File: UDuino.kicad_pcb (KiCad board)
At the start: 2 copper layers, 31 parts, among them J1 Screw_Terminal_01x04, U1 NAU8315YG, U2 DRV8833RTY, U3 NAU8315YG, U4 STM32L452VCTx

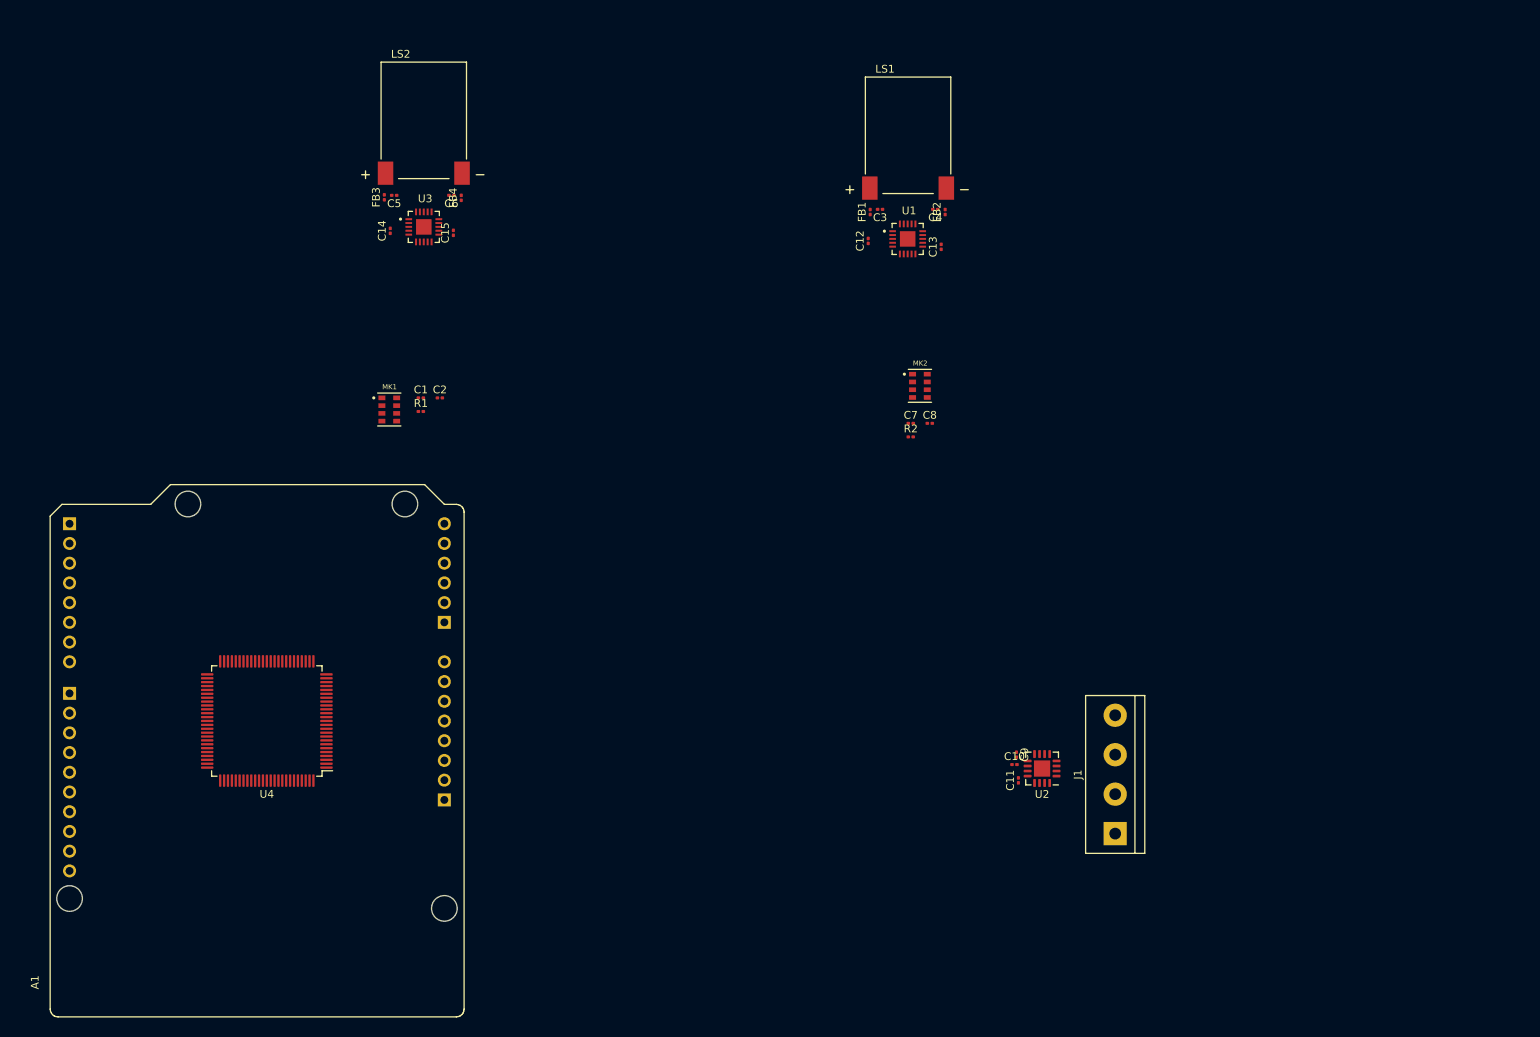
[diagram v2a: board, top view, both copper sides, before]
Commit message: Added Switches, Buttons, LEDs, 7Seg, LCD
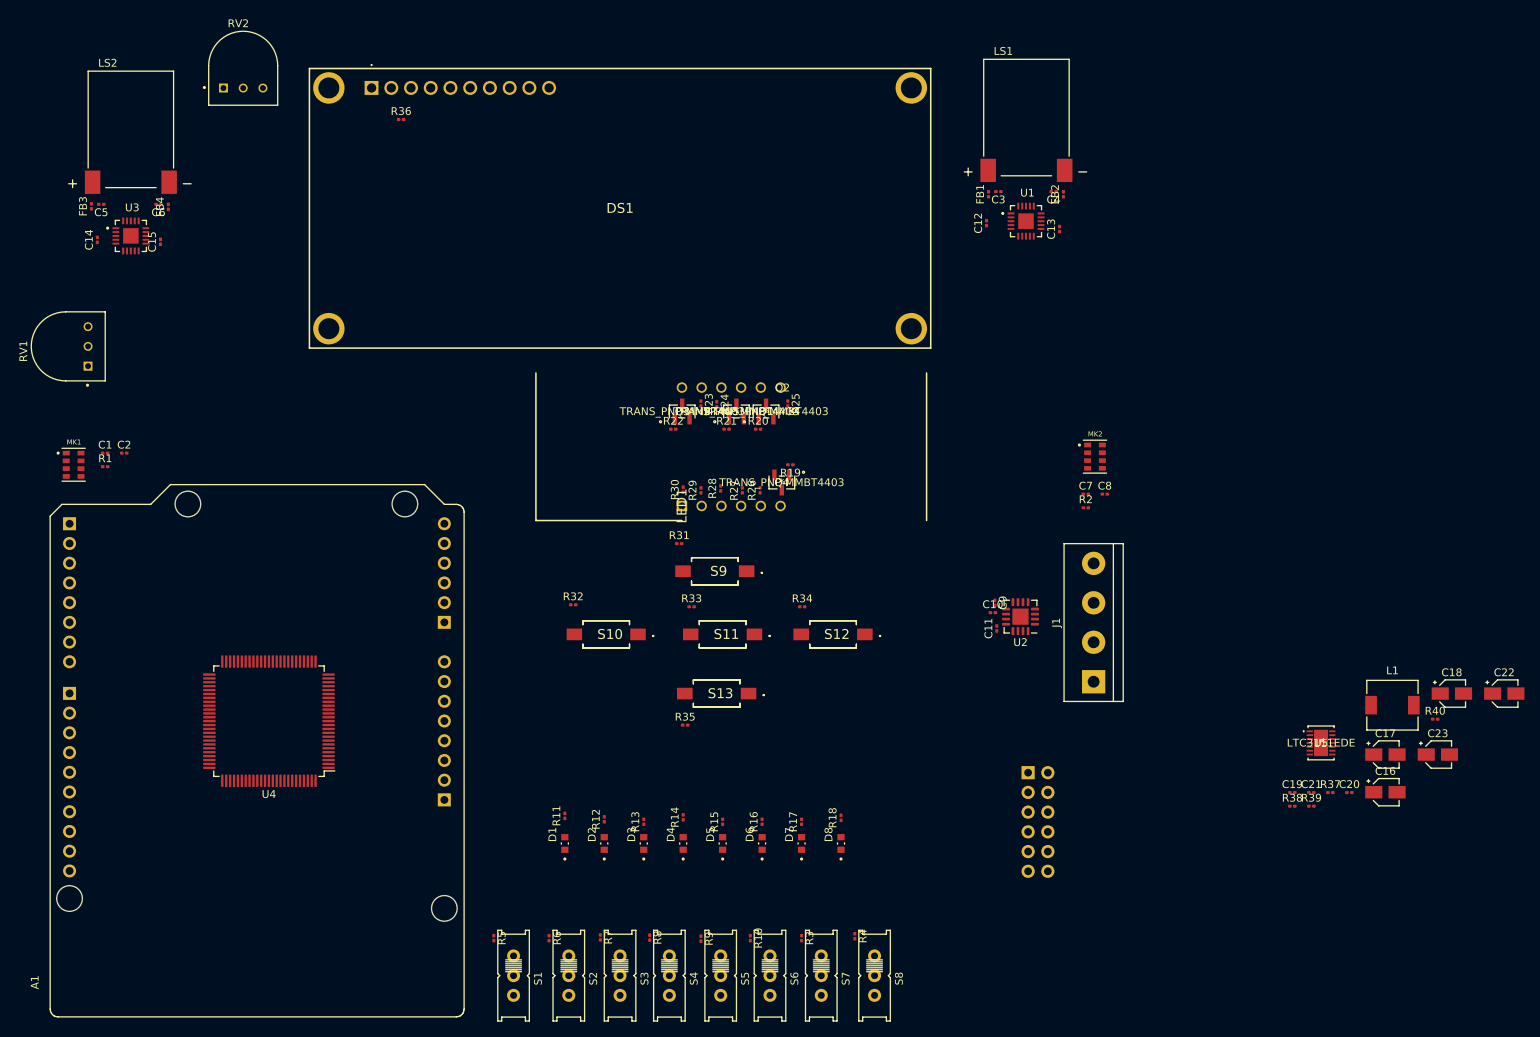
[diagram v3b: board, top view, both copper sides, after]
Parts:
- added C16: 27pF, Capacitor_SMD:CP_Elec_3x5.3, F.Cu at (201.2, 127.3)
- added C17: 600pF, Capacitor_SMD:CP_Elec_3x5.3, F.Cu at (201.2, 122.4)
- added C18: 27pF, Capacitor_SMD:CP_Elec_3x5.3, F.Cu at (209.7, 114.6)
- added C19: 0u1, Capacitor_SMD:C_0201_0603Metric, F.Cu at (189.2, 127.3)
- added C20: 0u1, Capacitor_SMD:C_0201_0603Metric, F.Cu at (196.5, 127.3)
- added C21: 1µF, Capacitor_SMD:C_0201_0603Metric, F.Cu at (191.6, 127.3)
- added C22: 33pF, Capacitor_SMD:CP_Elec_3x5.3, F.Cu at (216.5, 114.6)
- added C23: 22µF, Capacitor_SMD:CP_Elec_3x5.3, F.Cu at (207.9, 122.4)
- added D1: LTST-C190KRKT, Custom:LEDC1608X35N, F.Cu at (95.5, 133.9)
- added D2: LTST-C190KRKT, Custom:LEDC1608X35N, F.Cu at (100.6, 133.9)
- added D3: LTST-C190KRKT, Custom:LEDC1608X35N, F.Cu at (105.7, 133.9)
- added D4: LTST-C190KRKT, Custom:LEDC1608X35N, F.Cu at (110.7, 133.9)
- added D5: LTST-C190KRKT, Custom:LEDC1608X35N, F.Cu at (115.8, 133.9)
- added D6: LTST-C190KRKT, Custom:LEDC1608X35N, F.Cu at (120.9, 133.9)
- added D7: LTST-C190KRKT, Custom:LEDC1608X35N, F.Cu at (126.0, 133.9)
- added D8: LTST-C190KRKT, Custom:LEDC1608X35N, F.Cu at (131.1, 133.9)
- added DS1: AMC1602AR-B-Y6WFDY-SPI, Custom:AMC1602ARBY6WFDYSPI, F.Cu at (70.6, 36.6)
- added J2: PMOD1, Connector_PinSocket_2.54mm:PinSocket_2x06_P2.54mm_Horizontal, B.Cu at (155.2, 124.7)
- added L1: 4u7, Inductor_SMD:L_6.3x6.3_H3, F.Cu at (202.1, 116.1)
- added LED1: LDQ-M516RI, Custom:DIPS1524W50P254L5030H800Q12N, F.Cu at (110.6, 90.4)
- added Q1: TRANS_PNP-MMBT4403, Custom:MMBT4403LT3G, F.Cu at (121.4, 78.2)
- added Q2: TRANS_PNP-MMBT4403, Custom:MMBT4403LT3G, F.Cu at (117.6, 78.2)
- added Q3: TRANS_PNP-MMBT4403, Custom:MMBT4403LT3G, F.Cu at (110.6, 78.2)
- added Q4: TRANS_PNP-MMBT4403, Custom:MMBT4403LT3G, F.Cu at (123.4, 87.4)
- added R10: 10k, Resistor_SMD:R_0201_0603Metric, F.Cu at (119.4, 146.1)
- added R11: 220, Resistor_SMD:R_0201_0603Metric, F.Cu at (95.5, 130.3)
- added R12: 220, Resistor_SMD:R_0201_0603Metric, F.Cu at (100.6, 130.7)
- added R13: 220, Resistor_SMD:R_0201_0603Metric, F.Cu at (105.7, 131.1)
- added R14: 220, Resistor_SMD:R_0201_0603Metric, F.Cu at (110.7, 130.5)
- added R15: 220, Resistor_SMD:R_0201_0603Metric, F.Cu at (115.8, 131.1)
- added R16: 220, Resistor_SMD:R_0201_0603Metric, F.Cu at (120.9, 131.1)
- added R17: 220, Resistor_SMD:R_0201_0603Metric, F.Cu at (126.0, 131.1)
- added R18: 220, Resistor_SMD:R_0201_0603Metric, F.Cu at (131.1, 130.6)
- added R19: 1k, Resistor_SMD:R_0201_0603Metric, F.Cu at (124.6, 85.1)
- added R20: 1k, Resistor_SMD:R_0201_0603Metric, F.Cu at (120.4, 80.5)
- added R21: 1k, Resistor_SMD:R_0201_0603Metric, F.Cu at (116.3, 80.5)
- added R22: 1k, Resistor_SMD:R_0201_0603Metric, F.Cu at (109.5, 80.5)
- added R23: 220, Resistor_SMD:R_0201_0603Metric, F.Cu at (113.0, 77.2)
- added R24: 220, Resistor_SMD:R_0201_0603Metric, F.Cu at (115.1, 77.3)
- added R25: 220, Resistor_SMD:R_0201_0603Metric, F.Cu at (124.2, 77.2)
- added R26: 220, Resistor_SMD:R_0201_0603Metric, F.Cu at (120.7, 88.4)
- added R27: 220, Resistor_SMD:R_0201_0603Metric, F.Cu at (118.4, 88.4)
- added R28: 220, Resistor_SMD:R_0201_0603Metric, F.Cu at (115.6, 88.1)
- added R29: 220, Resistor_SMD:R_0201_0603Metric, F.Cu at (113.0, 88.4)
- added R3: 10k, Resistor_SMD:R_0201_0603Metric, F.Cu at (126.0, 146.1)
- added R30: 220, Resistor_SMD:R_0201_0603Metric, F.Cu at (110.7, 88.3)
- added R31: 10k, Resistor_SMD:R_0201_0603Metric, F.Cu at (110.2, 95.2)
- added R32: 10k, Resistor_SMD:R_0201_0603Metric, F.Cu at (96.6, 103.1)
- added R33: 10k, Resistor_SMD:R_0201_0603Metric, F.Cu at (111.8, 103.4)
- added R34: 10k, Resistor_SMD:R_0201_0603Metric, F.Cu at (126.1, 103.4)
- added R35: 10k, Resistor_SMD:R_0201_0603Metric, F.Cu at (111.0, 118.6)
- added R36: 50, Resistor_SMD:R_0201_0603Metric, F.Cu at (74.4, 40.6)
- added R37: 26.1k, Resistor_SMD:R_0201_0603Metric, F.Cu at (194.1, 127.3)
- added R38: 57.6k, Resistor_SMD:R_0201_0603Metric, F.Cu at (189.2, 129.1)
- added R39: 1M, Resistor_SMD:R_0201_0603Metric, F.Cu at (191.6, 129.1)
- added R4: 10k, Resistor_SMD:R_0201_0603Metric, F.Cu at (132.8, 145.8)
- added R40: 20k, Resistor_SMD:R_0201_0603Metric, F.Cu at (207.6, 117.9)
- added R5: 10k, Resistor_SMD:R_0201_0603Metric, F.Cu at (86.4, 146.1)
- added R6: 10k, Resistor_SMD:R_0201_0603Metric, F.Cu at (93.5, 146.1)
- added R7: 10k, Resistor_SMD:R_0201_0603Metric, F.Cu at (100.1, 146.0)
- added R8: 10k, Resistor_SMD:R_0201_0603Metric, F.Cu at (106.4, 146.0)
- added R9: 10k, Resistor_SMD:R_0201_0603Metric, F.Cu at (113.0, 146.1)
- added RV1: R_Potentiometer, Custom:TRIM_3352T-1-104LF, F.Cu at (31.2, 69.8)
- added RV2: 100k, Custom:TRIM_3352T-1-104LF, F.Cu at (54.1, 33.7)
- added S1: EG1218, Custom:EG1218, F.Cu at (88.9, 150.9)
- added S10: PTS636_SM43_SMTR_LFS, Custom:PTS636SM43SMTRLFS, F.Cu at (100.8, 106.9)
- added S11: PTS636_SM43_SMTR_LFS, Custom:PTS636SM43SMTRLFS, F.Cu at (115.8, 106.9)
- added S12: PTS636_SM43_SMTR_LFS, Custom:PTS636SM43SMTRLFS, F.Cu at (130.0, 106.9)
- added S13: PTS636_SM43_SMTR_LFS, Custom:PTS636SM43SMTRLFS, F.Cu at (115.1, 114.6)
- added S2: EG1218, Custom:EG1218, F.Cu at (96.0, 150.9)
- added S3: EG1218, Custom:EG1218, F.Cu at (102.6, 150.9)
- added S4: EG1218, Custom:EG1218, F.Cu at (109.0, 150.9)
- added S5: EG1218, Custom:EG1218, F.Cu at (115.6, 150.9)
- added S6: EG1218, Custom:EG1218, F.Cu at (121.9, 150.9)
- added S7: EG1218, Custom:EG1218, F.Cu at (128.5, 150.9)
- added S8: EG1218, Custom:EG1218, F.Cu at (135.4, 150.9)
- added S9: PTS636_SM43_SMTR_LFS, Custom:PTS636SM43SMTRLFS, F.Cu at (114.8, 98.8)
- added U5: LTC3111EDE, Custom:LTC3111EDE-TRPBF, F.Cu at (192.9, 120.9)
- moved C2 41.3 mm to (38.8, 83.6)
- moved C1 41.3 mm to (36.3, 83.6)
- moved R1 41.3 mm to (36.3, 85.3)
- moved MK1 41.3 mm to (32.3, 85.1)
- moved C5 37.7 mm to (35.8, 51.6)
- moved C6 37.7 mm to (43.2, 51.6)
- moved C14 37.7 mm to (35.3, 56.1)
- moved C15 37.7 mm to (43.4, 56.4)
- moved FB3 37.7 mm to (34.5, 51.8)
- moved FB4 37.7 mm to (44.5, 51.9)
- moved LS2 37.7 mm to (39.6, 41.9)
- moved U3 37.7 mm to (39.6, 55.6)
- moved MK2 24.3 mm to (163.8, 84.0)
- moved C7 24.3 mm to (162.6, 88.9)
- moved C8 24.3 mm to (165.0, 88.9)
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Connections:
- net Net-(A1-PadA0) renamed /A0
- net Net-(A1-PadA1) renamed /A1
- net Net-(A1-PadA2) renamed /A2
- net Net-(A1-PadA3) renamed /A3
- net Net-(A1-PadA4) renamed /A4
- net Net-(A1-PadA4)_1 renamed /I2C4_SDA
- net Net-(A1-PadA5) renamed /A5
- net Net-(A1-PadA5)_1 renamed /I2C4_SCL
- net Net-(A1-PadD2) renamed /D2
- net Net-(A1-PadD3) renamed /D3
- net Net-(A1-PadD4) renamed /D4
- net Net-(A1-PadD5) renamed /D5
- net Net-(U4-Pad45) renamed /D6
- net Net-(U4-Pad46) renamed /D7
- A1 pad 3V3: unconnected-(A1-Pad3V3) -> +3V3
- A1 pad 5V: unconnected-(A1-Pad5V) -> +5V
- A1 pad GND_1: unconnected-(A1-PadGND_1) -> GND
- A1 pad GND_2: unconnected-(A1-PadGND_2) -> GND
- MK1 pad 3: /SIA1_FS_B -> /SAI1_FS_A
- MK1 pad 6: /SIA1_SCK_B -> /SAI1_SCK_A
- MK2 pad 3: /SIA1_FS_B -> /SAI1_FS_A
- MK2 pad 6: /SIA1_SCK_B -> /SAI1_SCK_A
- U3 pad 13: /Speaker Right/GAIN -> /Speaker Left/GAIN
- U4 pad 1: unconnected-(U4-Pad1) -> /Motor/BIN2
- U4 pad 10: unconnected-(U4-Pad10) -> GND
- U4 pad 100: unconnected-(U4-Pad100) -> +3V3
- U4 pad 11: unconnected-(U4-Pad11) -> +3V3
- U4 pad 15: /Motor/AIN1 -> /LEDs/LED1
- U4 pad 16: /Motor/AIN2 -> /LEDs/LED2
- U4 pad 17: /Motor/BIN2 -> /LEDs/LED3
- U4 pad 18: /Motor/BIN1 -> /LEDs/LED4
- U4 pad 19: unconnected-(U4-Pad19) -> GND
- U4 pad 2: unconnected-(U4-Pad2) -> /Motor/BIN1
- U4 pad 22: unconnected-(U4-Pad22) -> +3V3
- U4 pad 27: unconnected-(U4-Pad27) -> GND
- U4 pad 28: unconnected-(U4-Pad28) -> +3V3
- U4 pad 33: unconnected-(U4-Pad33) -> /LEDs/LED5
- U4 pad 34: unconnected-(U4-Pad34) -> /LEDs/LED6
- U4 pad 35: unconnected-(U4-Pad35) -> /PMOD4
- U4 pad 36: unconnected-(U4-Pad36) -> /LCD/RS
- U4 pad 37: unconnected-(U4-Pad37) -> /LCD/CSB
- U4 pad 39: /SIA_SCK_B -> /PMOD_6
- U4 pad 40: /SIA1_FS_B -> /PMOD_7
- U4 pad 47: unconnected-(U4-Pad47) -> /Buttons/BT4
- U4 pad 48: unconnected-(U4-Pad48) -> /Buttons/BT5
- U4 pad 49: unconnected-(U4-Pad49) -> GND
- U4 pad 50: unconnected-(U4-Pad50) -> +3V3
- U4 pad 51: unconnected-(U4-Pad51) -> /7Seg/AN1
- U4 pad 52: unconnected-(U4-Pad52) -> /7Seg/AN2
- U4 pad 53: unconnected-(U4-Pad53) -> /7Seg/AN3
- U4 pad 54: unconnected-(U4-Pad54) -> /7Seg/AN4
- U4 pad 6: unconnected-(U4-Pad6) -> +3V3
- U4 pad 63: unconnected-(U4-Pad63) -> /LEDs/LED7
- U4 pad 64: unconnected-(U4-Pad64) -> /LEDs/LED8
- U4 pad 65: unconnected-(U4-Pad65) -> /7Seg/A
- U4 pad 66: unconnected-(U4-Pad66) -> /7Seg/B
- U4 pad 67: unconnected-(U4-Pad67) -> /PMOD_1
- U4 pad 68: unconnected-(U4-Pad68) -> /PMOD2
- U4 pad 69: unconnected-(U4-Pad69) -> /PMOD_3
- U4 pad 7: unconnected-(U4-Pad7) -> /7Seg/F
- U4 pad 70: unconnected-(U4-Pad70) -> /USB_DM
- U4 pad 71: unconnected-(U4-Pad71) -> /USB_DP
- U4 pad 72: unconnected-(U4-Pad72) -> /SYS_JTMS-SWDIO
- U4 pad 74: unconnected-(U4-Pad74) -> GND
- U4 pad 75: unconnected-(U4-Pad75) -> +3V3
- U4 pad 76: unconnected-(U4-Pad76) -> /SYS_JTCK-SWCLK
- U4 pad 77: unconnected-(U4-Pad77) -> /SYS_JTDI
- U4 pad 78: unconnected-(U4-Pad78) -> /7Seg/C
- U4 pad 79: unconnected-(U4-Pad79) -> /7Seg/D
- U4 pad 8: unconnected-(U4-Pad8) -> /7Seg/G
- U4 pad 80: unconnected-(U4-Pad80) -> /7Seg/E
- U4 pad 81: unconnected-(U4-Pad81) -> /SW1
- U4 pad 82: unconnected-(U4-Pad82) -> /SW2
- U4 pad 83: unconnected-(U4-Pad83) -> /SW3
- U4 pad 84: unconnected-(U4-Pad84) -> /SW4
- U4 pad 85: unconnected-(U4-Pad85) -> /SW5
- U4 pad 86: unconnected-(U4-Pad86) -> /SW6
- U4 pad 87: unconnected-(U4-Pad87) -> /SW7
- U4 pad 88: unconnected-(U4-Pad88) -> /SW8
- U4 pad 9: unconnected-(U4-Pad9) -> /7Seg/DP
- U4 pad 92: unconnected-(U4-Pad92) -> /PMOD_5
- U4 pad 93: unconnected-(U4-Pad93) -> /Buttons/BT1
- U4 pad 95: unconnected-(U4-Pad95) -> /Buttons/BT2
- U4 pad 96: unconnected-(U4-Pad96) -> /Buttons/BT3
- U4 pad 97: unconnected-(U4-Pad97) -> /Motor/AIN1
- U4 pad 98: unconnected-(U4-Pad98) -> /Motor/AIN2
- U4 pad 99: unconnected-(U4-Pad99) -> GND

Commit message: Update board design
5v and 3v3 power blocks wired up.
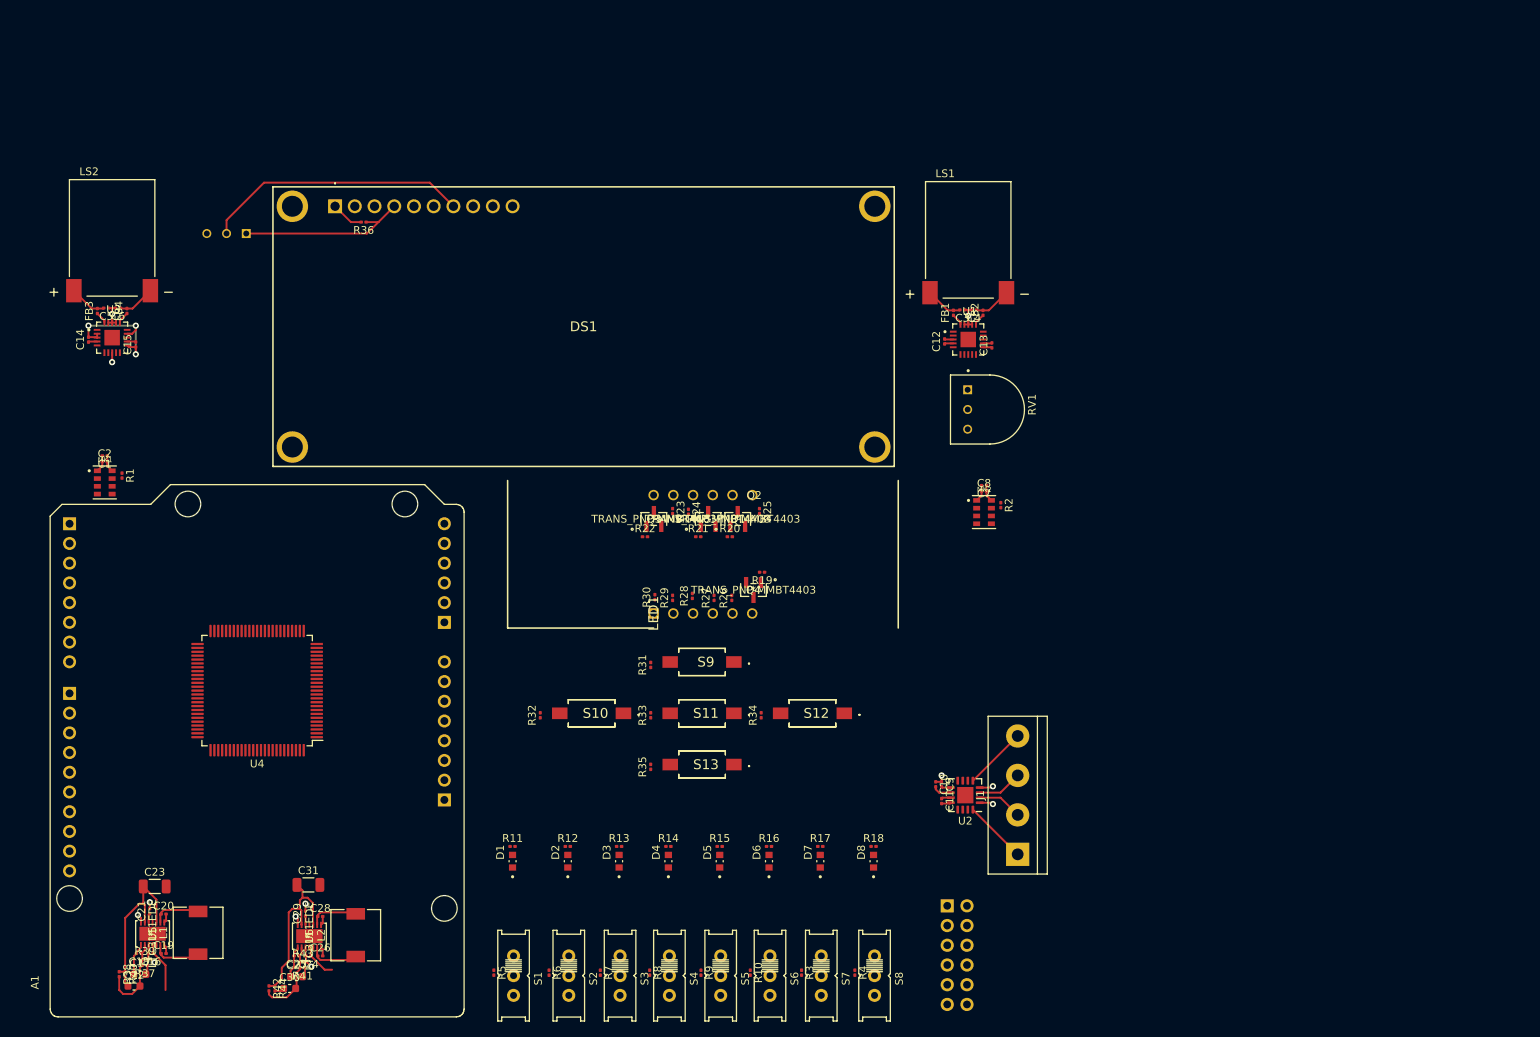
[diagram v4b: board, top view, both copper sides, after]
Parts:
- added C24: 27pF, Capacitor_SMD:C_0201_0603Metric, F.Cu at (62.5, 148.3)
- added C25: 27pF, Capacitor_SMD:C_0201_0603Metric, F.Cu at (61.0, 148.3)
- added C26: 0u1, Capacitor_SMD:C_0201_0603Metric, F.Cu at (64.0, 148.3)
- added C27: 680pF, Capacitor_SMD:C_0603_1608Metric, F.Cu at (61.0, 151.0)
- added C28: 0u1, Capacitor_SMD:C_0201_0603Metric, F.Cu at (64.0, 143.3)
- added C29: 1µF, Capacitor_SMD:C_0201_0603Metric, F.Cu at (62.1, 142.9)
- added C30: 33pF, Capacitor_SMD:C_0603_1608Metric, F.Cu at (60.1, 152.5)
- added C31: 22µF, Capacitor_SMD:C_1206_3216Metric, F.Cu at (62.5, 139.2)
- added L2: 4u7, Inductor_SMD:L_6.3x6.3_H3, F.Cu at (68.6, 145.7)
- added R41: 26.1k, Resistor_SMD:R_0201_0603Metric, F.Cu at (61.7, 149.9)
- added R42: 1M, Resistor_SMD:R_0201_0603Metric, F.Cu at (57.4, 152.5)
- added R43: 320k, Resistor_SMD:R_0201_0603Metric, F.Cu at (61.7, 149.1)
- added R44: 20k, Resistor_SMD:R_0201_0603Metric, F.Cu at (58.2, 152.5)
- added U6: LTC3111EDE, Custom:LTC3111EDE-TRPBF, F.Cu at (62.6, 145.8)
- C16, C18: footprint Capacitor_SMD:CP_Elec_3x5.3 -> Capacitor_SMD:C_0201_0603Metric
- C17: value 600pF -> 680pF; footprint Capacitor_SMD:CP_Elec_3x5.3 -> Capacitor_SMD:C_0603_1608Metric
- C22: footprint Capacitor_SMD:CP_Elec_3x5.3 -> Capacitor_SMD:C_0603_1608Metric
- C23: footprint Capacitor_SMD:CP_Elec_3x5.3 -> Capacitor_SMD:C_1206_3216Metric
- R38: value 57.6k -> 1M
- R39: value 1M -> 191k
- RV2: moved to B.Cu
- moved C22 180.4 mm to (40.0, 152.2)
- moved C18 172.3 mm to (40.7, 148.0), turned to 180 degrees
- moved R40 171.9 mm to (38.9, 150.7), turned to -90 degrees
- moved C23 166.1 mm to (42.7, 139.4)
- moved C17 162.9 mm to (40.8, 150.7)
- moved C16 160.3 mm to (42.2, 148.0), turned to 180 degrees
- moved L1 156.6 mm to (48.3, 145.4), turned to 90 degrees
- moved R37 154.3 mm to (41.4, 149.6), turned to 180 degrees
- moved C20 153.5 mm to (43.8, 142.9)
- moved R38 152.6 mm to (38.1, 150.7), turned to -90 degrees
- moved U5 152.5 mm to (42.4, 145.5), turned to 90 degrees
- moved R39 151.5 mm to (41.4, 148.8)
- moved C21 150.3 mm to (42.1, 142.6), turned to 90 degrees
- moved C19 146.8 mm to (43.8, 148.0)
- moved RV1 119.3 mm to (150.2, 78.0), turned to -90 degrees
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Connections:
- C17 pad 1: Net-(C17-Pad1) -> Net-(U5-Pad1)
- C18 pad 1: Net-(C17-Pad1) -> Net-(U5-Pad2)
- C18 pad 2: Net-(C18-Pad2) -> Net-(U5-Pad1)
- C22 pad 2: Net-(C18-Pad2) -> Net-(U5-Pad2)
- R37 pad 2: Net-(C18-Pad2) -> Net-(U5-Pad2)
- R38 pad 2: Net-(C18-Pad2) -> Net-(U5-Pad2)
- R39 pad 1: Net-(C18-Pad2) -> Net-(U5-Pad2)
- U5 pad 1: Net-(C18-Pad2) -> Net-(U5-Pad1)
- U5 pad 13: /Power 5V/PWM/SYNC -> +5V
- U5 pad 2: Net-(C17-Pad1) -> Net-(U5-Pad2)
- U5 pad 4: /Power 5V/RUN -> VDD
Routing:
- net +3V3: track 0.00 -> 46.3 mm, vias 0 -> 3
- net +5V: track 0.00 -> 45.4 mm
- net Net-(DS1-Pad7): track 0.00 -> 34.2 mm
- net GND: track 0.00 -> 34.2 mm, vias 0 -> 12
- net VDD: track 0.00 -> 12.2 mm
- net Net-(U5-Pad2): track 0.00 -> 10.7 mm
- net Net-(C25-Pad1): track 0.00 -> 10.2 mm
- net /Motor/BOUT1: track 0.00 -> 8.16 mm
- net /Motor/AOUT1: track 0.00 -> 8.16 mm
- net Net-(C26-Pad1): track 0.00 -> 6.52 mm
- net Net-(C19-Pad1): track 0.00 -> 6.45 mm
- net Net-(C28-Pad1): track 0.00 -> 6.42 mm
- net Net-(C20-Pad1): track 0.00 -> 6.34 mm
- net /Motor/AOUT2: track 0.00 -> 5.80 mm
- net /Motor/BOUT2: track 0.00 -> 5.80 mm
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
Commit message: Routing of some wires
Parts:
- added J3: Conn_01x04_Male, Connector_PinHeader_2.54mm:PinHeader_1x04_P2.54mm_Vertical, F.Cu at (37.6, 104.1)
- added J4: Conn_01x04_Male, Connector_PinHeader_2.54mm:PinHeader_1x04_P2.54mm_Vertical, F.Cu at (37.6, 99.1)
- added J5: Conn_01x03_Male, Connector_PinHeader_2.54mm:PinHeader_1x03_P2.54mm_Vertical, F.Cu at (68.5, 101.6)
- added J6: Conn_01x03_Male, Connector_PinHeader_2.54mm:PinHeader_1x03_P2.54mm_Vertical, F.Cu at (68.5, 96.5)
- moved J2 25.2 mm to (146.4, 116.7)
- moved S9 16.8 mm to (99.1, 119.6)
- moved S12 16.7 mm to (113.3, 126.1)
- moved R34 16.7 mm to (106.7, 126.4)
- moved R31 16.7 mm to (92.5, 119.9)
- moved R32 14.9 mm to (106.7, 113.3)
- moved R35 14.9 mm to (120.9, 119.9)
- moved S10 14.9 mm to (113.3, 113.0)
- moved S13 14.9 mm to (127.5, 119.6)
- moved C11 14.7 mm to (145.7, 143.0)
- moved J1 14.7 mm to (155.5, 149.9)
- moved U2 14.7 mm to (148.7, 142.2)
- moved C10 14.7 mm to (144.9, 140.8)
- moved C9 14.7 mm to (145.7, 140.8)
- moved U4 8.13 mm to (55.9, 122.3)
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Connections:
- DS1 pad 6: /LCD/SID -> /SPI3_MOSI
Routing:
- net +3V3: track 46.3 -> 162.9 mm
- net /Motor/AIN1: track 0.00 -> 97.1 mm
- net /Motor/AIN2: track 0.00 -> 94.9 mm
- net /Motor/BIN1: track 0.00 -> 93.1 mm
- net /Motor/BIN2: track 0.00 -> 92.2 mm
- net /SW8: track 0.00 -> 86.4 mm
- net /SW7: track 0.00 -> 80.2 mm
- net /SW6: track 0.00 -> 74.2 mm
- net /SW5: track 0.00 -> 68.4 mm
- net /SW4: track 0.00 -> 62.4 mm
- net /SW3: track 0.00 -> 56.6 mm
- net /LEDs/LED4: track 0.00 -> 51.9 mm
- net /SW2: track 0.00 -> 50.6 mm
- net /LEDs/LED8: track 0.00 -> 49.8 mm
- net /LEDs/LED3: track 0.00 -> 45.4 mm
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
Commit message: 06/12/2022
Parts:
- moved RV1 27.5 mm to (141.6, 53.7), turned to 0 degrees
- moved C15 13.7 mm to (48.8, 80.4)
- moved LS2 13.7 mm to (45.7, 66.7)
- moved C14 13.7 mm to (42.7, 79.8)
- moved C5 13.7 mm to (45.0, 75.7)
- moved C6 13.7 mm to (46.5, 75.7)
- moved FB3 13.7 mm to (43.8, 76.1)
- moved FB4 13.7 mm to (47.6, 76.1)
- moved U3 13.7 mm to (45.7, 79.5)
- moved C12 12.9 mm to (137.4, 80.0)
- moved C13 12.9 mm to (143.5, 80.5)
- moved C3 12.9 mm to (139.7, 75.9)
- moved C4 12.9 mm to (141.2, 75.9)
- moved FB1 12.9 mm to (138.6, 76.3)
- moved FB2 12.9 mm to (142.4, 76.3)
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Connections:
- A1 pad D3: /D3 -> /D4
- J3 pad 1: +3V3 -> GND
- J3 pad 2: /D4 -> +3V3
- J3 pad 3: /D5 -> /D4
- J3 pad 4: GND -> /D5
- J4 pad 1: +3V3 -> GND
- J4 pad 2: /D2 -> +3V3
- J4 pad 3: /D3 -> /D2
- J4 pad 4: GND -> /D4
- J5 pad 1: +3V3 -> GND
- J5 pad 2: /A2 -> +3V3
- J5 pad 3: GND -> /A2
- J6 pad 1: +3V3 -> GND
- J6 pad 2: /A3 -> +3V3
- J6 pad 3: GND -> /A3
- U4 pad 42: /D3 -> /D4
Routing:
- net /Buttons/BT5: track 2.52 -> 91.1 mm, vias 0 -> 2
- net /SPI3_MOSI: track 1.43 -> 84.1 mm, vias 0 -> 2
- net /SPI3_SCK: track 1.32 -> 83.4 mm, vias 0 -> 2
- net /7Seg/C: track 0.00 -> 80.4 mm, vias 0 -> 2
- net /LCD/RS: track 0.00 -> 72.1 mm
- net /7Seg/D: track 0.00 -> 71.8 mm, vias 0 -> 2
- net /LCD/CSB: track 0.00 -> 71.2 mm
- net /Buttons/BT2: track 2.54 -> 72.4 mm, vias 0 -> 2
- net /7Seg/E: track 0.00 -> 69.1 mm, vias 0 -> 4
- net /Buttons/BT4: track 2.53 -> 71.4 mm, vias 0 -> 2
- net /7Seg/G: track 0.00 -> 65.7 mm, vias 0 -> 2
- net /7Seg/F: track 0.00 -> 64.5 mm, vias 0 -> 2
- net /Buttons/BT3: track 2.53 -> 63.6 mm, vias 0 -> 2
- net /7Seg/DP: track 0.00 -> 59.9 mm, vias 0 -> 2
- net /Buttons/BT1: track 2.53 -> 50.4 mm, vias 0 -> 2
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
